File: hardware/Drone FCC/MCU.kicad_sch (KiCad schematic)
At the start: 34 parts, among them SW1 SW_MEC_5E, U3 STM32F746ZGTx, Y1 12MHz, Y2 32.768kHz

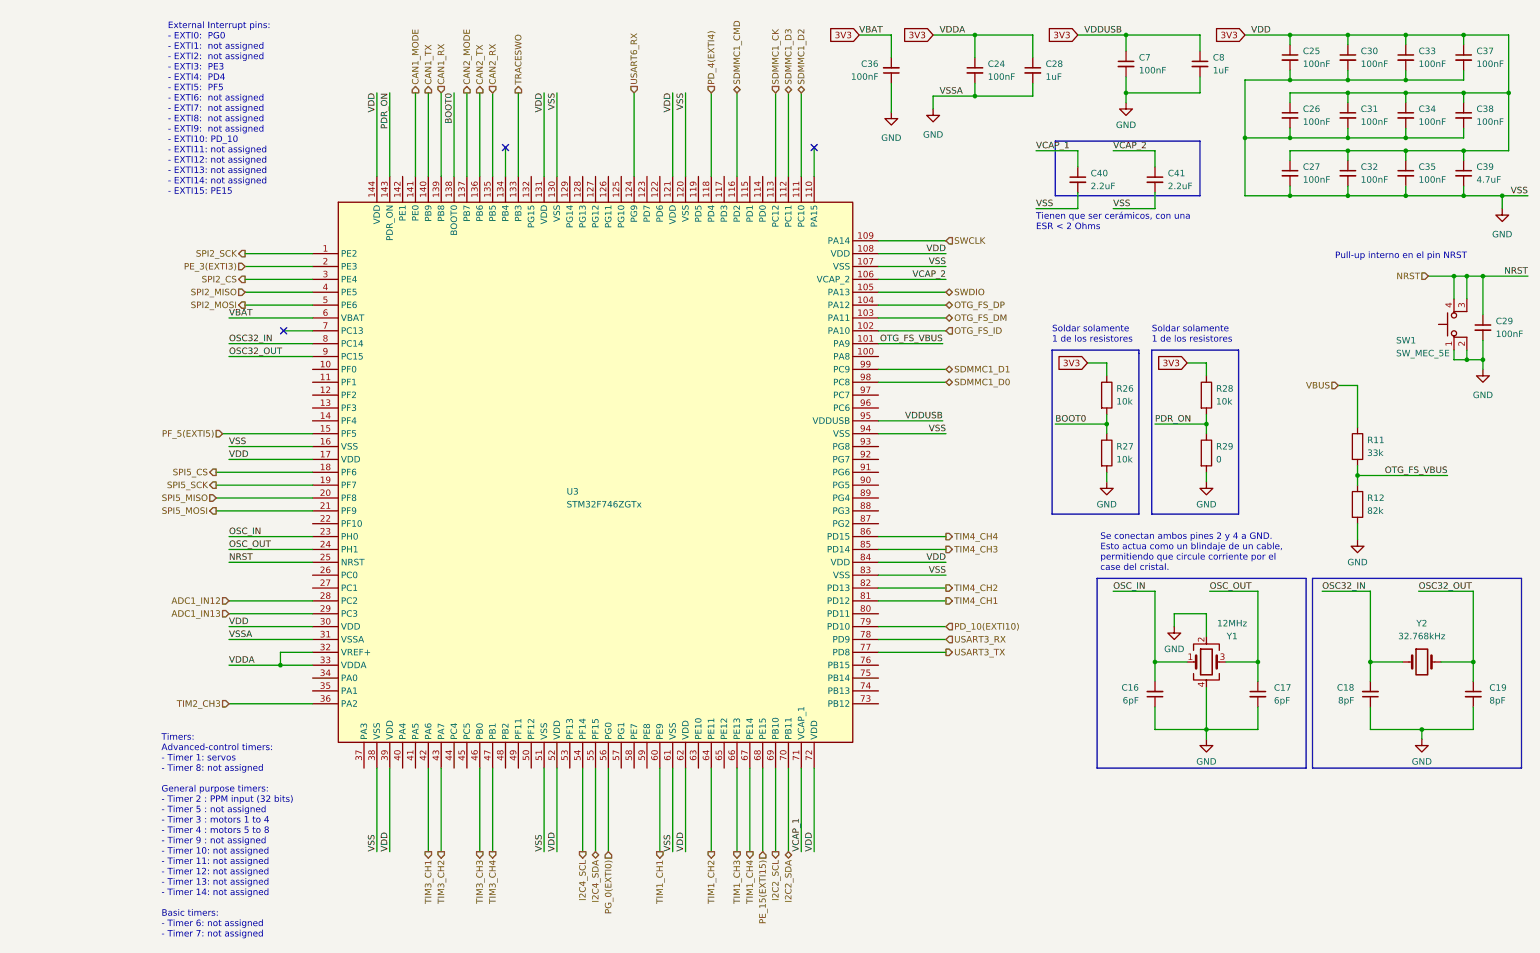
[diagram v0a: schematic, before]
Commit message: re enumeration of components
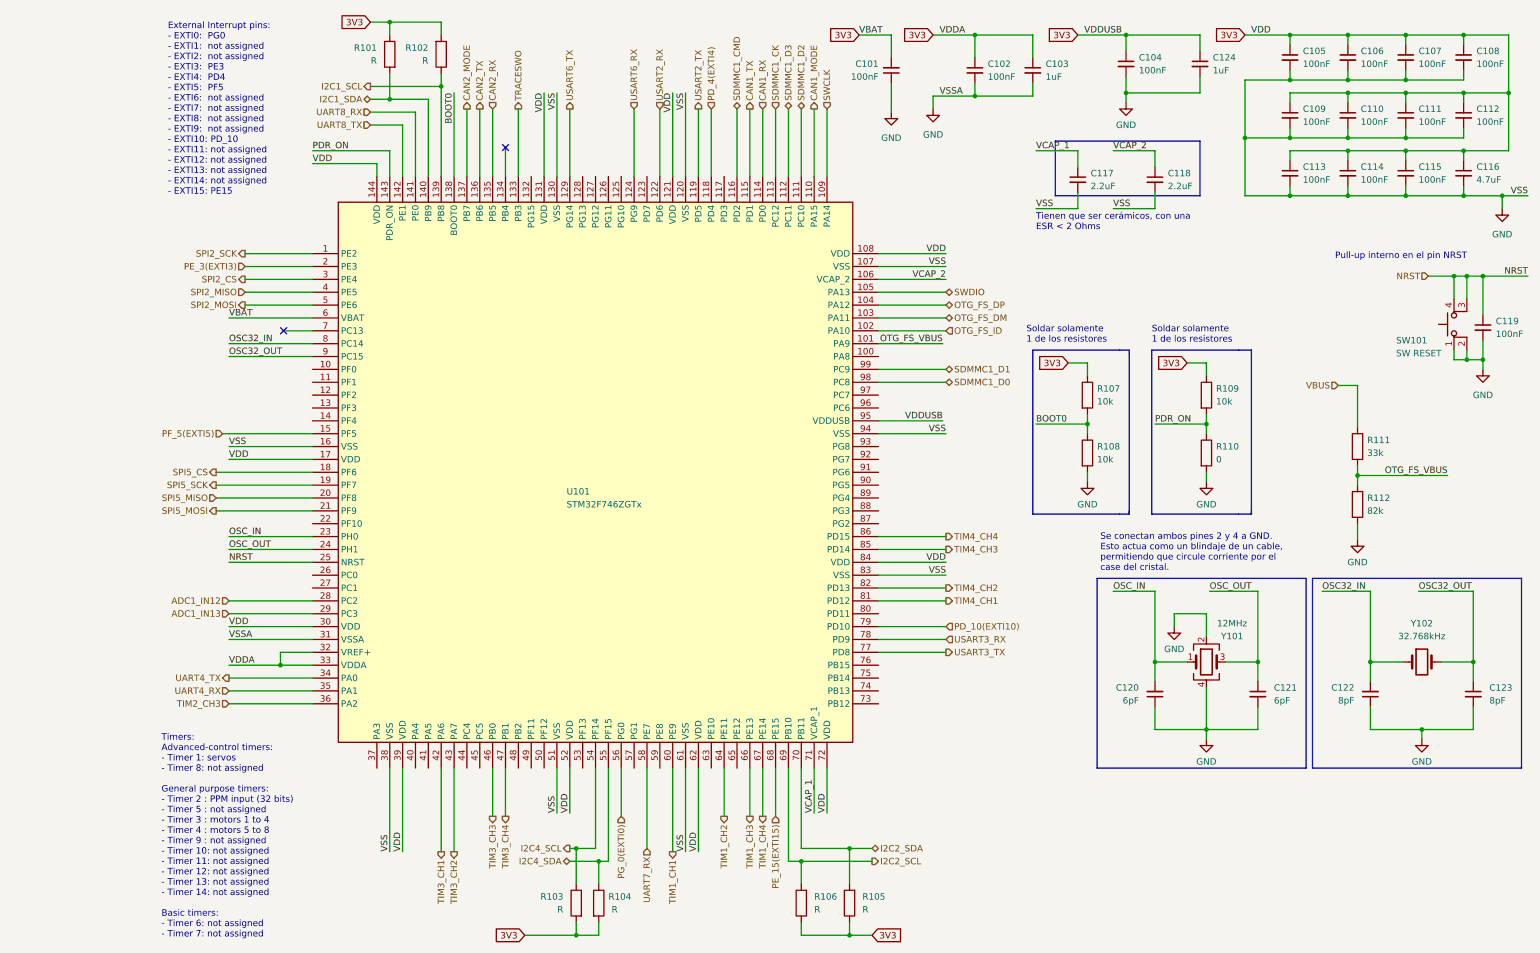
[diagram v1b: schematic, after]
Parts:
- added R101, R102, R103, R104, R105, R106: R, symbol Device:R
- SW101: renamed from SW1; value SW_MEC_5E -> SW RESET
- renumbered C36 to C101, C24 to C102, C28 to C103, C7 to C104, C25 to C105, C30 to C106, C33 to C107, C37 to C108, C26 to C109, C31 to C110, C34 to C111, C38 to C112, C27 to C113, C32 to C114, C35 to C115, C39 to C116, C40 to C117, C41 to C118, C29 to C119, C16 to C120, C17 to C121, C18 to C122, C19 to C123, C8 to C124, R26 to R107, R27 to R108, R28 to R109, R29 to R110, R11 to R111, R12 to R112, U3 to U101, Y1 to Y101, Y2 to Y102
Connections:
- net 3V3: now also R101.1, R102.2, R103.2, R104.2, R105.1, R106.1
- net CAN1_MODE: now also U101.110 (PA15); no longer U101.141 (PE0)
- net CAN1_RX: now also U101.114 (PD0); no longer U101.139 (PB8)
- net CAN1_TX: now also U101.115 (PD1); no longer U101.140 (PB9)
- net I2C2_SCL: now also R106.2
- net I2C2_SDA: now also R105.2
- net I2C4_SCL: now also R103.1
- net I2C4_SDA: now also R104.1
- net USART2_TX: now reaches U101.119 (PD5)
- net USART2_RX: now reaches U101.122 (PD6)
- net USART6_TX: now reaches U101.129 (PG14)
- net UART8_TX: now reaches U101.142 (PE1)
- net UART4_TX: now reaches U101.34 (PA0)
- net UART4_RX: now reaches U101.35 (PA1)
- net UART7_RX: now reaches U101.58 (PE7)
- new net I2C1_SCL: R102.1, U101.139 (PB8)
- new net I2C1_SDA: R101.2, U101.140 (PB9)
- new net UART8_RX: U101.141 (PE0)
- no-connect marks 3 -> 2
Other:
- moved on the sheet: R107, R108

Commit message: start routing
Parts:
- removed R101, R102: R, symbol Device:R
- removed SW101: SW RESET, Button_Switch_SMD:SW_SPST_TL3305A, symbol Switch:SW_MEC_5E
- added SW101: SW RESET, Button_Switch_SMD:SW_SPST_TL3305A, symbol Switch:SW_Push
- C101, C102, C104, C105, C106, C107, C108, C109, C110, C111, C112, C113, C114, C115, C119: footprint (none) -> Capacitor_SMD:C_0603_1608Metric_Pad1.08x0.95mm_HandSolder
- C103, C116, C124: footprint (none) -> Capacitor_SMD:C_0805_2012Metric_Pad1.18x1.45mm_HandSolder
- C117, C118: footprint (none) -> Capacitor_SMD:C_1206_3216Metric_Pad1.33x1.80mm_HandSolder
- C120, C121, C122, C123: footprint (none) -> Capacitor_SMD:C_0402_1005Metric_Pad0.74x0.62mm_HandSolder
- R103, R104, R105, R106, R107, R108, R109, R110, R111, R112: footprint (none) -> Resistor_SMD:R_0402_1005Metric_Pad0.72x0.64mm_HandSolder
- Y101: footprint (none) -> ECS-120-8-33Q-RES-TR:XTAL_ECS-120-8-33Q-RES-TR
- Y102: footprint (none) -> ECS-.327-9-34QCS-TR9:ECS-.327-9-34QN-TR
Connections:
- net I2C1_SCL is gone; now on net CAN1_RX: U101.139 (PB8)
- net I2C1_SDA is gone; now on net CAN1_TX: U101.140 (PB9)
- net CAN1_MODE: now also U101.137 (PB7); no longer U101.110 (PA15)
- net CAN1_RX: no longer U101.114 (PD0)
- net CAN1_TX: no longer U101.115 (PD1)
- net CAN2_MODE: now also U101.134 (PB4); no longer U101.137 (PB7)
- net GND: now also SW101.1
- net NRST: now also SW101.2
- no-connect marks 2 -> 5

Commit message: continued preliminar routing
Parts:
- C101, C102, C104, C105, C106, C107, C108, C109, C110, C111, C112, C113, C114, C115: footprint Capacitor_SMD:C_0603_1608Metric_Pad1.08x0.95mm_HandSolder -> Capacitor_SMD:C_0402_1005Metric_Pad0.74x0.62mm_HandSolder
- C116: footprint Capacitor_SMD:C_0805_2012Metric_Pad1.18x1.45mm_HandSolder -> Capacitor_SMD:C_0603_1608Metric_Pad1.08x0.95mm_HandSolder
- C117, C118: footprint Capacitor_SMD:C_1206_3216Metric_Pad1.33x1.80mm_HandSolder -> Capacitor_SMD:C_0603_1608Metric_Pad1.08x0.95mm_HandSolder
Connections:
- net SPI2_CS: now also U101.73 (PB12); no longer U101.3 (PE4)
- net SPI2_MISO: now also U101.75 (PB14); no longer U101.4 (PE5)
- net SPI2_MOSI: now also U101.76 (PB15); no longer U101.5 (PE6)
- net SPI2_SCK: now also U101.74 (PB13); no longer U101.1 (PE2)
- net UART4_RX: no longer U101.35 (PA1)
- net UART4_TX: no longer U101.34 (PA0)
- net TIM2_CH4: now reaches U101.37 (PA3)
- new net TIM2_CH1: U101.34 (PA0)
- new net TIM2_CH2: U101.35 (PA1)

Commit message: routing: connected everything
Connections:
- net ADC1_IN12: now also U101.40 (PA4); no longer U101.28 (PC2)
- net ADC1_IN13: now also U101.41 (PA5); no longer U101.29 (PC3)
- net PG_2(EXTI2): now reaches U101.87 (PG2)
- net PE_3(EXTI3): no longer names the net of U101.2 (PE3)
- net PG_0(EXTI0): no longer names the net of U101.56 (PG0)
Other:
- note added: "External Interrupt pins: - EXTI0: not assigned - EXTI1: not assigned - EXTI2: PG2 - EXTI3: not assigned - EXTI4: PD4 - EXTI5: PF5 - EXTI6: not assigned - EXTI7: not assigned - EXTI8: not assigned - EXTI9: not assigned - EXTI10: PD10 - EXTI11: not assigned - EXTI12: not assigned - EXTI13: not assigned - EXTI14: not assigned - EXTI15: PE15"
- note removed: "External Interrupt pins: - EXTI0: PG0 - EXTI1: not assigned - EXTI2: not assigned - EXTI3: PE3 - EXTI4: PD4 - EXTI5: PF5 - EXTI6: not assigned - EXTI7: not assigned - EXTI8: not assigned - EXTI9: not assigned - EXTI10: PD_10 - EXTI11: not assigned - EXTI12: not assigned - EXTI13: not assigned - EXTI14: not assigned - EXTI15: PE15"
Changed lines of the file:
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@@
+    (stroke (width 0) (type default) (color 0 0 0 0))
+  )
+  (wire (pts (xy 154.94 114.3) (xy 168.275 114.3))
     (stroke (width 0) (type default) (color 0 0 0 0))
   )
@@
     (stroke (width 0) (type default) (color 0 0 0 0))
   )
-  (wire (pts (xy 26.67 129.54) (xy 43.18 129.54))
+  (wire (pts (xy 63.5 179.07) (xy 63.5 162.56))
     (stroke (width 0) (type default) (color 0 0 0 0))
   )
@@
     (stroke (width 0) (type default) (color 0 0 0 0))
   )
-  (wire (pts (xy 104.14 162.56) (xy 104.14 172.085))
-    (stroke (width 0) (type default) (color 0 0 0 0))
-  )
   (wire (pts (xy 149.225 193.04) (xy 149.225 195.58))
     (stroke (width 0) (type default) (color 0 0 0 0))
@@
     (stroke (width 0) (type default) (color 0 0 0 0))
   )
-  (wire (pts (xy 29.845 63.5) (xy 43.18 63.5))
-    (stroke (width 0) (type default) (color 0 0 0 0))
-  )
   (wire (pts (xy 219.71 154.94) (xy 229.87 154.94))
     (stroke (width 0) (type default) (color 0 0 0 0))
@@
     (stroke (width 0) (type default) (color 0 0 0 0))
   )
-  (wire (pts (xy 26.67 132.08) (xy 43.18 132.08))
+  (wire (pts (xy 66.04 179.07) (xy 66.04 162.56))
     (stroke (width 0) (type default) (color 0 0 0 0))
   )
@@
     (effects (font (size 1.27 1.27)) (justify left bottom))
   )
-  (text "External Interrupt pins:\n- EXTI0:  PG0\n- EXTI1:  not assigned\n- EXTI2:  not assigned\n- EXTI3:  PE3\n- EXTI4:  PD4\n- EXTI5:  PF5\n- EXTI6:  not assigned\n- EXTI7:  not assigned\n- EXTI8:  not assigned\n- EXTI9:  not assigned\n- EXTI10: PD_10\n- EXTI11: not assigned\n- EXTI12: not assigned\n- EXTI13: not assigned\n- EXTI14: not assigned\n- EXTI15: PE15"
-    (at 14.605 49.53 0)
+  (text "External Interrupt pins:\n- EXTI0:  not assigned\n- EXTI1:  not assigned\n- EXTI2:  PG2\n- EXTI3:  not assigned\n- EXTI4:  PD4\n- EXTI5:  PF5\n- EXTI6:  not assigned\n- EXTI7:  not assigned\n- EXTI8:  not assigned\n- EXTI9:  not assigned\n- EXTI10: PD10\n- EXTI11: not assigned\n- EXTI12: not assigned\n- EXTI13: not assigned\n- EXTI14: not assigned\n- EXTI15: PE15"
+    (at 15.24 48.26 0)
     (effects (font (size 1.27 1.27)) (justify left bottom))
   )
@@
     (effects (font (size 1.27 1.27)) (justify left))
   )
-  (hierarchical_label "ADC1_IN13" (shape input) (at 26.67 132.08 180)
+  (hierarchical_label "ADC1_IN13" (shape input) (at 66.04 179.07 270)
     (effects (font (size 1.27 1.27)) (justify right))
   )
@@
     (effects (font (size 1.27 1.27)) (justify left))
   )
-  (hierarchical_label "PG_0(EXTI0)" (shape input) (at 104.14 172.085 270)
-    (effects (font (size 1.27 1.27)) (justify right))
-  )
   (hierarchical_label "PD_10(EXTI10)" (shape input) (at 168.275 134.62 0)
     (effects (font (size 1.27 1.27)) (justify left))
   )
-  (hierarchical_label "ADC1_IN12" (shape input) (at 26.67 129.54 180)
+  (hierarchical_label "ADC1_IN12" (shape input) (at 63.5 179.07 270)
     (effects (font (size 1.27 1.27)) (justify right))
   )
@@
     (effects (font (size 1.27 1.27)) (justify right))
   )
+  (hierarchical_label "PG_2(EXTI2)" (shape input) (at 168.275 114.3 0)
+    (effects (font (size 1.27 1.27)) (justify left))
+  )
   (hierarchical_label "TIM1_CH3" (shape output) (at 129.54 172.085 270)
     (effects (font (size 1.27 1.27)) (justify right))
@@
     (effects (font (size 1.27 1.27)) (justify right))
   )
-  (hierarchical_label "PE_3(EXTI3)" (shape input) (at 29.845 63.5 180)
-    (effects (font (size 1.27 1.27)) (justify right))
-  )
